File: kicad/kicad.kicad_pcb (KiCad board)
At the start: 2 copper layers, 315 x 123 mm, 54 parts, among them J1 Conn_01x16_Pin, K0 !,,,,,,1, K1 ",,,,,,2, K10 *,,,,,,:, K11 =,,,,,,-, K12 Break, K13 Up, K14 Q, K15 W, K16 E, K17 R, K18 T, K19 Y, K2 #,,,,,,3, K20 U, K21 I, K22 O, K23 P, K24 @, K25 Left, K26 Right, K27 Down, K28 A, K29 S, K3 $,,,,,,4, K30 D, K31 F, K32 G, K33 H, K34 J, K35 K, K36 L, K37 +,,,,,,;, K38 ENTER, K39 CLEAR, K4 %,,,,,,5, K40 SHIFT, K41 Z, K42 X, K43 C, K44 V, K45 B, K46 N, K47 M, K48 <,,,,,,,, K49 >,,,,,,., K5 &,,,,,,6, K50 ?,,,,,,/, K51 SHIFT, K52 Blank, K6 ',,,,,,7, K7 (,,,,,,8, K8 ),,,,,,9, K9 0

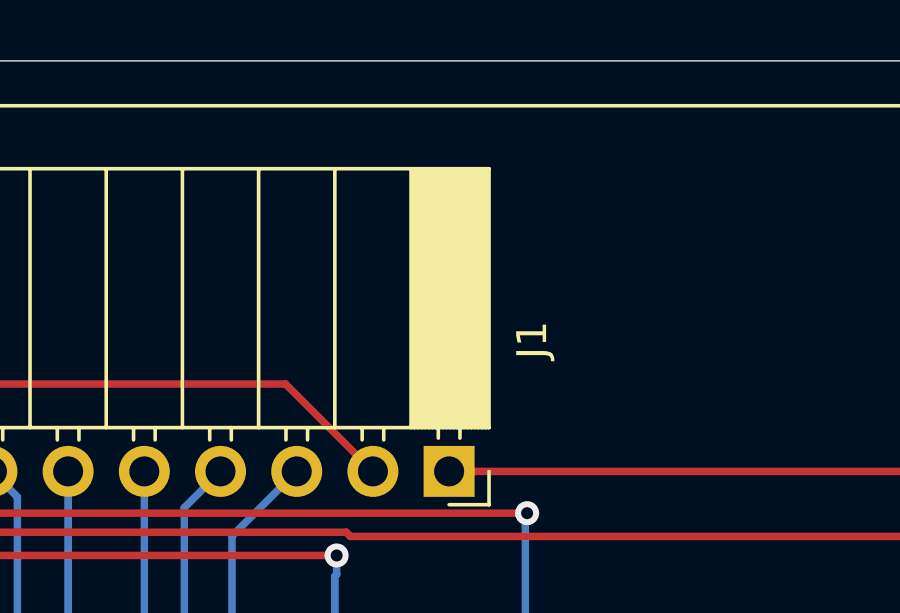
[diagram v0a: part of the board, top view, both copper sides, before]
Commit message: Remove slightly misleading pin-1 marking
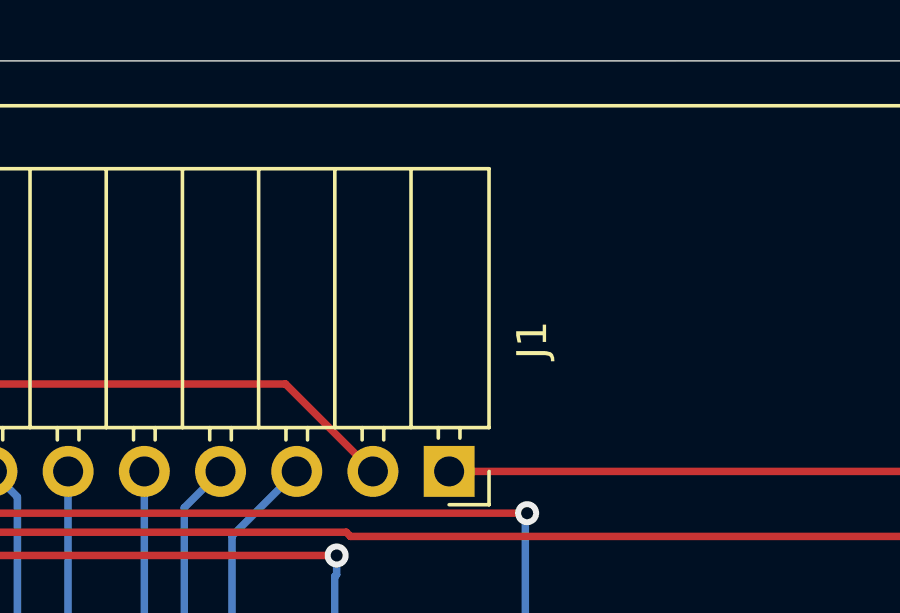
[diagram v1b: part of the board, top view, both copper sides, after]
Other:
- rule pad_to_mask_clearance: 0.051 -> 0
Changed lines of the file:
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@@
 	)
 	(setup
-		(pad_to_mask_clearance 0.051)
-		(solder_mask_min_width 0.25)
+		(pad_to_mask_clearance 0)
 		(allow_soldermask_bridges_in_footprints no)
 		(pcbplotparams
@@
 			(sketchpadsonfab no)
 			(subtractmaskfromsilk no)
-			(outputformat 4)
+			(outputformat 1)
 			(mirror no)
 			(drillshape 0)
 			(scaleselection 1)
-			(outputdirectory "")
+			(outputdirectory "plot")
 		)
 	)
@@
 		)
 		(fp_line
-			(start -10.09 1.1519)
-			(end -1.46 1.1519)
-			(stroke
-				(width 0.12)
-				(type solid)
-			)
-			(layer "F.SilkS")
-		)
-		(fp_line
-			(start -10.09 1.033805)
-			(end -1.46 1.033805)
-			(stroke
-				(width 0.12)
-				(type solid)
-			)
-			(layer "F.SilkS")
-		)
-		(fp_line
-			(start -10.09 0.91571)
-			(end -1.46 0.91571)
-			(stroke
-				(width 0.12)
-				(type solid)
-			)
-			(layer "F.SilkS")
-		)
-		(fp_line
-			(start -10.09 0.797615)
-			(end -1.46 0.797615)
-			(stroke
-				(width 0.12)
-				(type solid)
-			)
-			(layer "F.SilkS")
-		)
-		(fp_line
-			(start -10.09 0.67952)
-			(end -1.46 0.67952)
-			(stroke
-				(width 0.12)
-				(type solid)
-			)
-			(layer "F.SilkS")
-		)
-		(fp_line
-			(start -10.09 0.561425)
-			(end -1.46 0.561425)
-			(stroke
-				(width 0.12)
-				(type solid)
-			)
-			(layer "F.SilkS")
-		)
-		(fp_line
-			(start -10.09 0.44333)
-			(end -1.46 0.44333)
-			(stroke
-				(width 0.12)
-				(type solid)
-			)
-			(layer "F.SilkS")
-		)
-		(fp_line
 			(start -1.46 0.36)
 			(end -1.11 0.36)
@@
 		)
 		(fp_line
-			(start -10.09 0.325235)
-			(end -1.46 0.325235)
-			(stroke
-				(width 0.12)
-				(type solid)
-			)
-			(layer "F.SilkS")
-		)
-		(fp_line
-			(start -10.09 0.20714)
-			(end -1.46 0.20714)
-			(stroke
-				(width 0.12)
-				(type solid)
-			)
-			(layer "F.SilkS")
-		)
-		(fp_line
-			(start -10.09 0.089045)
-			(end -1.46 0.089045)
-			(stroke
-				(width 0.12)
-				(type solid)
-			)
-			(layer "F.SilkS")
-		)
-		(fp_line
-			(start -10.09 -0.02905)
-			(end -1.46 -0.02905)
-			(stroke
-				(width 0.12)
-				(type solid)
-			)
-			(layer "F.SilkS")
-		)
-		(fp_line
-			(start -10.09 -0.147145)
-			(end -1.46 -0.147145)
-			(stroke
-				(width 0.12)
-				(type solid)
-			)
-			(layer "F.SilkS")
-		)
-		(fp_line
-			(start -10.09 -0.26524)
-			(end -1.46 -0.26524)
-			(stroke
-				(width 0.12)
-				(type solid)
-			)
-			(layer "F.SilkS")
-		)
-		(fp_line
 			(start -1.46 -0.36)
 			(end -1.11 -0.36)
 			(stroke
 				(width 0.12)
-				(type solid)
-			)
-			(layer "F.SilkS")
-		)
-		(fp_line
-			(start -10.09 -0.383335)
-			(end -1.46 -0.383335)
-			(stroke
-				(width 0.12)
-				(type solid)
-			)
-			(layer "F.SilkS")
-		)
-		(fp_line
-			(start -10.09 -0.50143)
-			(end -1.46 -0.50143)
-			(stroke
-				(width 0.12)
-				(type solid)
-			)
-			(layer "F.SilkS")
-		)
-		(fp_line
-			(start -10.09 -0.619525)
-			(end -1.46 -0.619525)
-			(stroke
-				(width 0.12)
-				(type solid)
-			)
-			(layer "F.SilkS")
-		)
-		(fp_line
-			(start -10.09 -0.73762)
-			(end -1.46 -0.73762)
-			(stroke
-				(width 0.12)
-				(type solid)
-			)
-			(layer "F.SilkS")
-		)
-		(fp_line
-			(start -10.09 -0.855715)
-			(end -1.46 -0.855715)
-			(stroke
-				(width 0.12)
-				(type solid)
-			)
-			(layer "F.SilkS")
-		)
-		(fp_line
-			(start -10.09 -0.97381)
-			(end -1.46 -0.97381)
-			(stroke
-				(width 0.12)
-				(type solid)
-			)
-			(layer "F.SilkS")
-		)
-		(fp_line
-			(start -10.09 -1.091905)
-			(end -1.46 -1.091905)
-			(stroke
-				(width 0.12)
-				(type solid)
-			)
-			(layer "F.SilkS")
-		)
-		(fp_line
-			(start -10.09 -1.21)
-			(end -1.46 -1.21)
-			(stroke
-				(width 0.12)

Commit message: Bump entire keyboard usable area up a little bit
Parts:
- moved K27 1.36 mm to (112.0, 133.3)
- moved K28 1.36 mm to (131.1, 133.3)
- moved K29 1.36 mm to (150.1, 133.3)
- moved K30 1.36 mm to (169.2, 133.3)
- moved K31 1.36 mm to (188.2, 133.3)
- moved K32 1.36 mm to (207.3, 133.3)
- moved K33 1.36 mm to (226.3, 133.3)
- moved K34 1.36 mm to (245.4, 133.3)
- moved K35 1.36 mm to (264.4, 133.3)
- moved K36 1.36 mm to (283.5, 133.3)
- moved K37 1.36 mm to (302.5, 133.3)
- moved K38 1.36 mm to (333.5, 133.3)
- moved K39 1.36 mm to (364.4, 133.3)
- moved K52 1.36 mm to (228.7, 171.4)
- moved J1 1.36 mm to (247.6, 86.6)
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
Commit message: Prepare v2 number
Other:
- board text added: "coco keyboard insert v2 leadedsolder.com 2024"
- board text removed: "coco keyboard insert v1 leadedsolder.com 2024"
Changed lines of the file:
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@@
 		)
 	)
-	(gr_text "coco keyboard insert v1\nleadedsolder.com 2024"
+	(gr_text "coco keyboard insert v2\nleadedsolder.com 2024"
 		(at 366.5 192 0)
 		(layer "F.SilkS")

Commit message: Add F-board pull-up
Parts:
- added RN1: 4.7kΩ, Resistor_THT:R_Array_SIP9, B.Cu at (301.0, 86.4)
- added TP12: +5V input, Connector_PinHeader_2.54mm:PinHeader_1x01_P2.54mm_Horizontal, F.Cu at (295.3, 86.3)
- moved J1 62.9 mm to (184.7, 86.6)
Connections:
- J1 pad 14: unconnected-(J1-Pin_14-Pad14) -> /Key
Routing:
- net /Key: track 0.00 -> 172.4 mm, vias 0 -> 2
- net /Row2: track 203.8 -> 348.6 mm, vias 1 -> 3
- net /Row6: track 215.6 -> 311.6 mm, vias 2 -> 3
- net /Row4: track 349.0 -> 433.7 mm, vias 4 -> 7
- net /Row5: track 264.5 -> 319.3 mm, vias 0 -> 3
- net /Row3: track 268.8 -> 323.3 mm, vias 1 -> 3
- net /Row7: track 450.3 -> 501.4 mm, vias 2 -> 4
- net /Row1: track 337.6 -> 371.9 mm, vias 4 -> 5
- net /Col2: track 380.2 -> 412.7 mm, vias 6 -> 7
- net /Col3: track 432.1 -> 399.7 mm
- net /Col1: track 325.8 -> 346.8 mm, vias 5 -> 7
- net /Col4: track 326.9 -> 307.3 mm, vias 5 -> 6
- net /Col8: track 467.9 -> 486.4 mm
- net /Col5: track 291.5 -> 275.9 mm, vias 4 -> 3
- net /Col6: track 300.4 -> 310.1 mm, vias 5 -> 7
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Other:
- board text added: "+5V"

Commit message: Fix Spacebar
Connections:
- K52 pad 2: /Row5 -> /Row4
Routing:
- net /Row5: track 319.3 -> 281.9 mm
- net /Row4: track 433.7 -> 468.1 mm, vias 7 -> 8

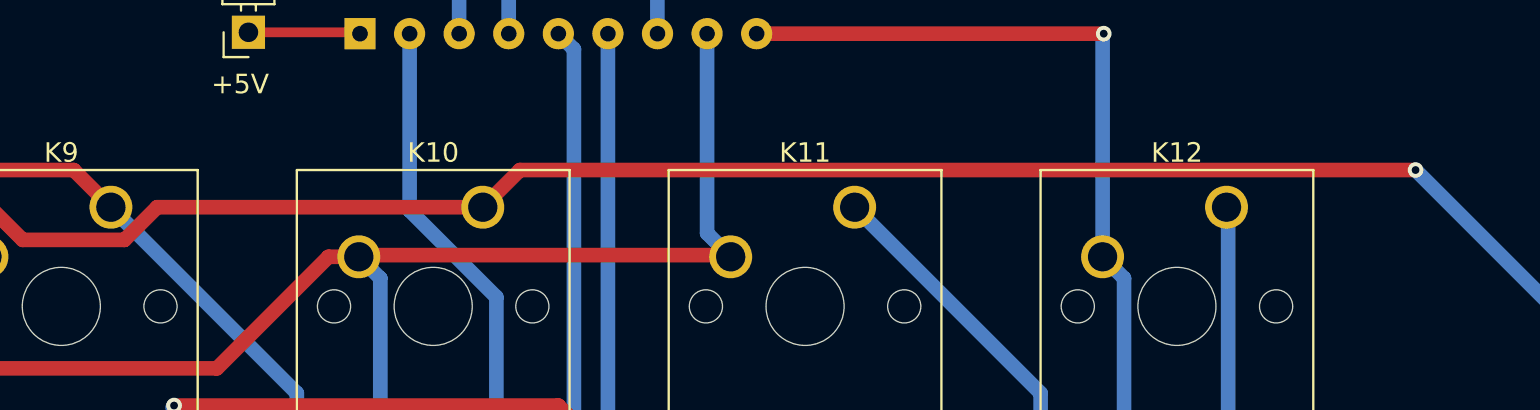
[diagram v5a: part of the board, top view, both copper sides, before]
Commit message: Fix asterisk key
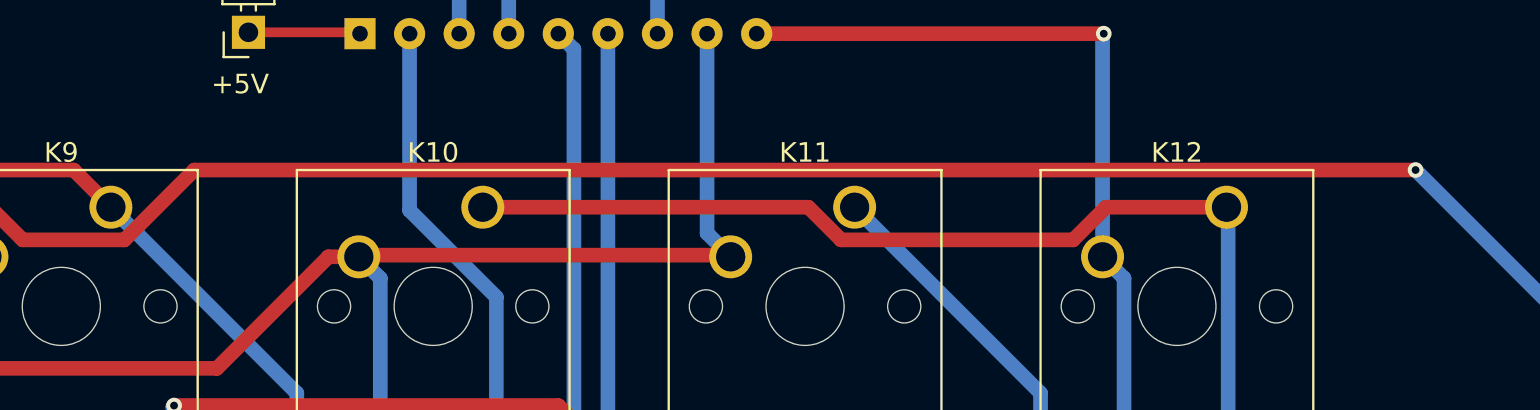
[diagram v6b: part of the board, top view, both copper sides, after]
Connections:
- K10 pad 1: /Col2 -> /Col3
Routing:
- net /Col3: track 399.7 -> 439.2 mm
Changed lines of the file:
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@@
 			(layers "*.Cu" "*.Mask")
 			(remove_unused_layers no)
-			(net 15 "/Col2")
+			(net 9 "/Col3")
 			(pinfunction "1")
 			(pintype "passive")
@@
 	)
 	(segment
+		(start 323.960658 95.25)
+		(end 325.635658 96.925)
+		(width 0.75)
+		(layer "F.Cu")
+		(net 9)
+	)
+	(segment
 		(start 217.268216 124.46)
 		(end 245.843216 124.46)
@@
 	)
 	(segment
+		(start 337.525658 96.925)
+		(end 339.200658 95.25)
+		(width 0.75)
+		(layer "F.Cu")
+		(net 9)
+	)
+	(segment
 		(start 135.829466 95.25)
 		(end 137.504466 93.575)
@@
 	)
 	(segment
+		(start 325.635658 96.925)
+		(end 337.525658 96.925)
+		(width 0.75)
+		(layer "F.Cu")
+		(net 9)
+	)
+	(segment
+		(start 339.200658 95.25)
+		(end 345.379466 95.25)
+		(width 0.75)
+		(layer "F.Cu")
+		(net 9)
+	)
+	(segment
 		(start 345.538216 129.54)
 		(end 345.278216 129.28)
@@
 	)
 	(segment
+		(start 307.279466 95.25)
+		(end 323.960658 95.25)
+		(width 0.75)
+		(layer "F.Cu")
+		(net 9)
+	)
+	(segment
 		(start 182.113216 93.575)
 		(end 182.343216 93.345)
@@
 	)
 	(segment
-		(start 288.923274 96.925)
-		(end 283.713216 96.925)
-		(width 0.75)
-		(layer "F.Cu")
-		(net 15)
-	)
-	(segment
-		(start 309.184466 93.345)
-		(end 307.279466 95.25)
+		(start 282.038216 95.25)
+		(end 269.179466 95.25)
 		(width 0.75)
 		(layer "F.Cu")
@@
 	)
 	(segment
-		(start 282.038216 95.25)
-		(end 269.179466 95.25)
+		(start 292.503274 93.345)
+		(end 288.923274 96.925)
 		(width 0.75)
 		(layer "F.Cu")
@@
 	)
 	(segment
-		(start 355.063216 93.345)
-		(end 309.184466 93.345)
+		(start 288.923274 96.925)
+		(end 283.713216 96.925)
 		(width 0.75)
 		(layer "F.Cu")
@@
 	)
 	(segment
-		(start 290.598274 95.25)
-		(end 288.923274 96.925)
+		(start 237.584569 114.3)
+		(end 239.259569 112.625)
 		(width 0.75)
 		(layer "F.Cu")
@@
 	)
 	(segment
-		(start 237.584569 114.3)
-		(end 239.259569 112.625)
+		(start 283.713216 96.925)
+		(end 282.038216 95.25)
 		(width 0.75)
 		(layer "F.Cu")
@@
 	)
 	(segment
-		(start 283.713216 96.925)
-		(end 282.038216 95.25)
-		(width 0.75)
-		(layer "F.Cu")
-		(net 15)
-	)
-	(segment
-		(start 307.279466 95.25)
-		(end 290.598274 95.25)
+		(start 355.063216 93.345)
+		(end 292.503274 93.345)
 		(width 0.75)
 		(layer "F.Cu")
